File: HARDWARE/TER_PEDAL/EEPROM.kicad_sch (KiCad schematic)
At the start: 1 part, among them U9 AT24CS02-STUM

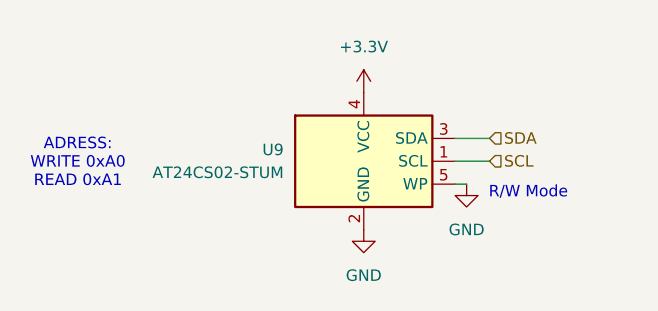
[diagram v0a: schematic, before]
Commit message: EEPROM añadida
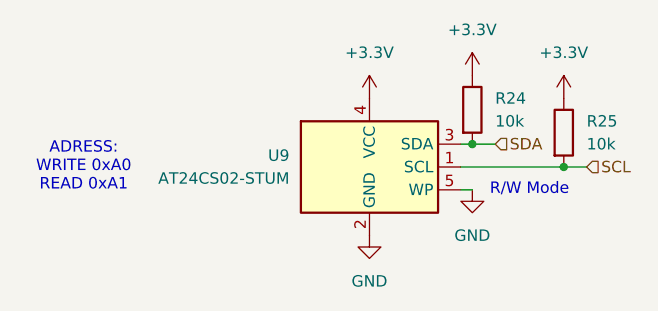
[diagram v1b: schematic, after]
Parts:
- added R24, R25: 10k, Resistor_SMD:R_0603_1608Metric, symbol Device:R
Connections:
- net +3.3V: now also R24.1, R25.1
- net SCL: now also R25.2
- net SDA: now also R24.2
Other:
- moved on the sheet: U9
